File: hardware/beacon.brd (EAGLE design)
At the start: 65.5 x 96.5 mm, 26 parts, among them IC1 LM1117SX-3.3, Q1 BC850SMD, Q2 BC850SMD, Q3 12MHz, U1 ESP-12F, X1 MINI-USB-UX60A-MB-5ST

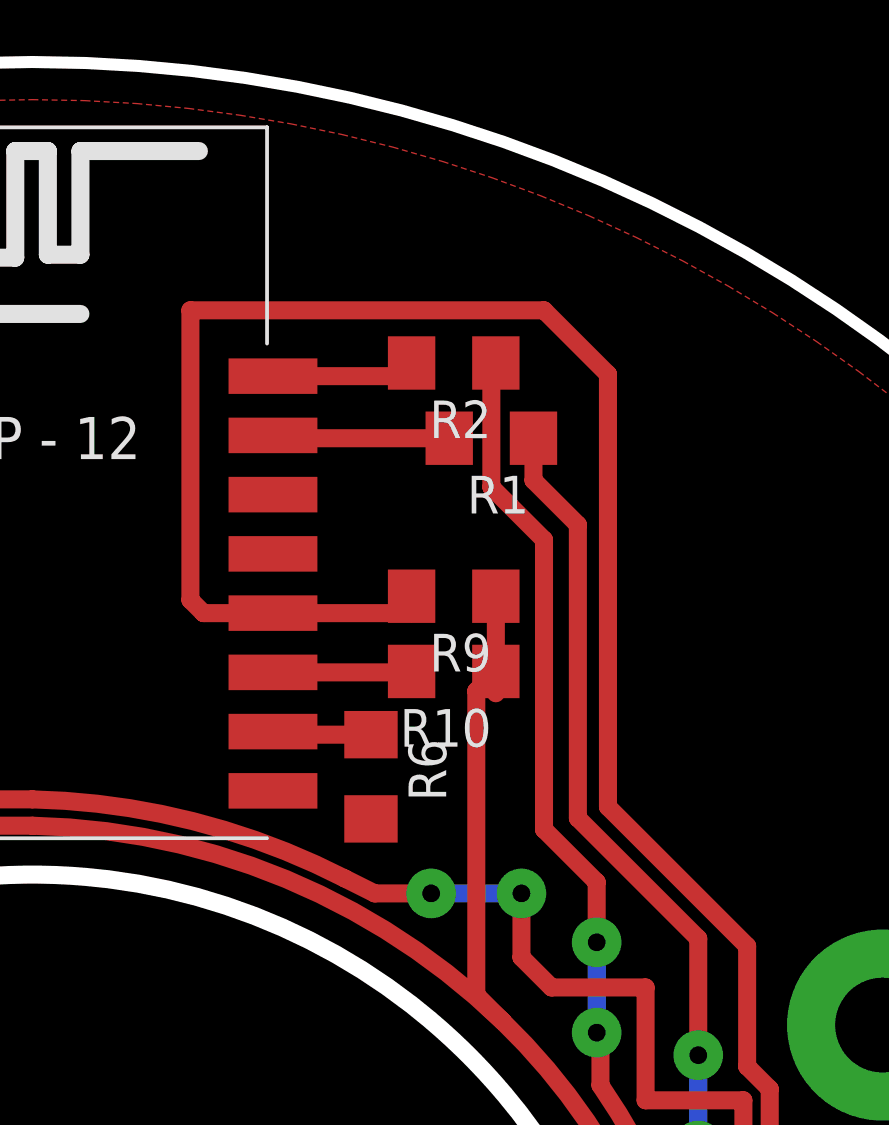
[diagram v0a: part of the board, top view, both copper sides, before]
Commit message: add test pads
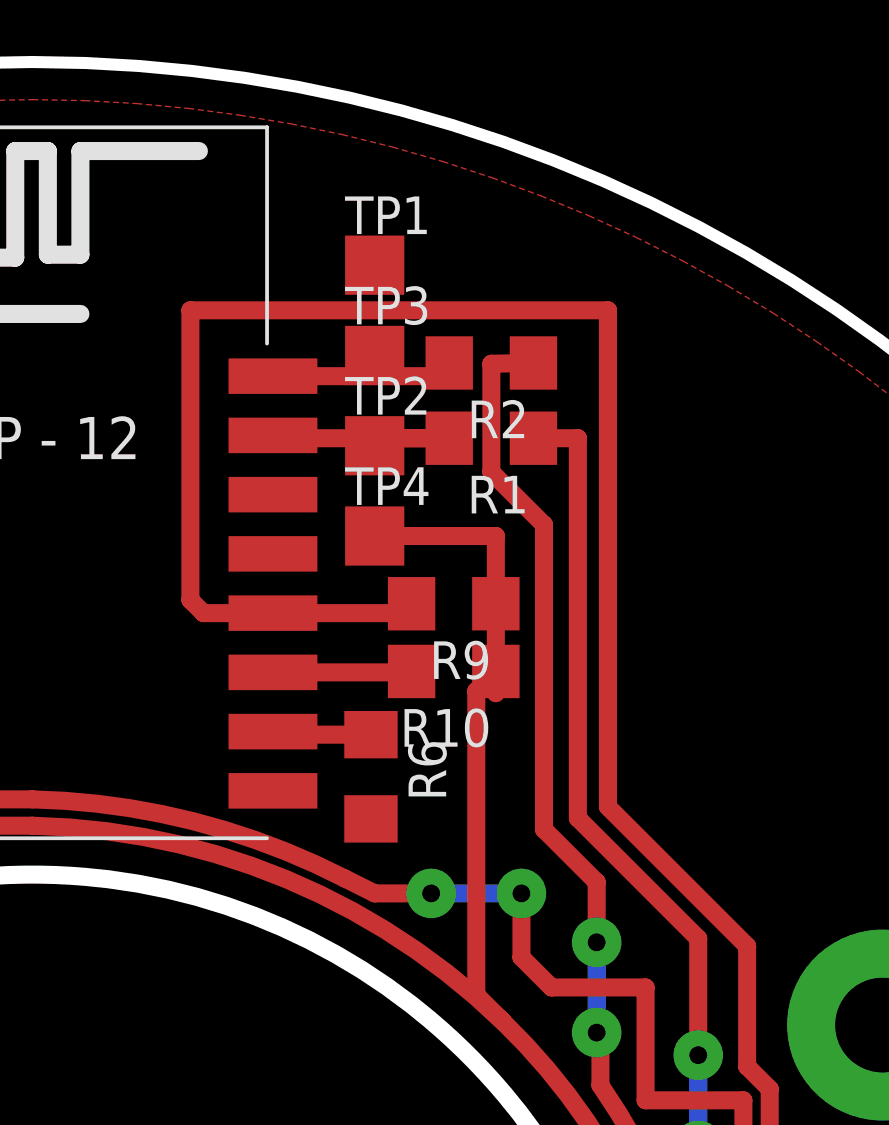
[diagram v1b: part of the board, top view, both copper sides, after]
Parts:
- added TP1, TP2, TP3, TP4: TPSQTP20SQ, testpad:TP20SQ
- moved R2 1.27 mm to (15.5, 38.1)
- moved R9 0.25 mm to (14.2, 30.0)
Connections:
- net +3V3: now also TP4.TP
- net GND: now also TP1.TP
- net RX: now also TP3.TP
- net TX: now also TP2.TP
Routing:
- net +3V3: track 221.6 -> 227.7 mm
- net TX: track 6.05 -> 8.81 mm
- net RX: track 5.12 -> 7.08 mm
- net N$2: track 85.8 -> 87.1 mm
- net GPIO0: track 109.4 -> 110.4 mm
- net N$1: track 82.8 -> 83.7 mm
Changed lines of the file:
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@@
 <element name="R1" library="rcl" package="R1206" value="470" x="15.494" y="35.56" rot="R180"/>
 <element name="R10" library="rcl" package="R1206" value="10k" x="14.224" y="27.686" rot="R180"/>
-<element name="R2" library="rcl" package="R1206" value="470" x="14.224" y="38.1" rot="R180"/>
+<element name="R2" library="rcl" package="R1206" value="470" x="15.494" y="38.1" rot="R180"/>
 <element name="R4" library="rcl" package="R1206" value="10k" x="26.1366" y="-34.9758" rot="R90"/>
 <element name="R5" library="rcl" package="R1206" value="10k" x="22.987" y="-37.211" rot="R90"/>
@@
 <element name="R7" library="rcl" package="R1206" value="10k" x="-13.589" y="30.988"/>
 <element name="R8" library="rcl" package="R1206" value="10k" x="-13.589" y="35.56"/>
-<element name="R9" library="rcl" package="R1206" value="10k" x="14.224" y="30.226" rot="R180"/>
+<element name="R9" library="rcl" package="R1206" value="10k" x="14.224" y="29.972" rot="R180"/>
 <element name="RESET" library="switch-omron" package="B3F-10XX" value="" x="-14.989309375" y="41.125021875" rot="R200">
 <attribute name="MF" value="" x="-14.989309375" y="41.125021875" size="1.778" layer="27" rot="R200" display="off"/>
@@
 <attribute name="OC_FARNELL" value="unknown" x="0" y="-41.91" size="1.778" layer="27" rot="R90" display="off"/>
 <attribute name="OC_NEWARK" value="unknown" x="0" y="-41.91" size="1.778" layer="27" rot="R90" display="off"/>
+</element>
+<element name="TP1" library="testpad" package="TP20SQ" value="TPSQTP20SQ" x="11.557" y="41.402">
+<attribute name="TP_SIGNAL_NAME" value="" x="11.557" y="41.402" size="1.778" layer="27" display="off"/>
+</element>
+<element name="TP2" library="testpad" package="TP20SQ" value="TPSQTP20SQ" x="11.557" y="35.306">
+<attribute name="TP_SIGNAL_NAME" value="" x="11.557" y="35.306" size="1.778" layer="27" display="off"/>
+</element>
+<element name="TP3" library="testpad" package="TP20SQ" value="TPSQTP20SQ" x="11.557" y="38.354">
+<attribute name="TP_SIGNAL_NAME" value="" x="11.557" y="38.354" size="1.778" layer="27" display="off"/>
+</element>
+<element name="TP4" library="testpad" package="TP20SQ" value="TPSQTP20SQ" x="11.557" y="32.258">
+<attribute name="TP_SIGNAL_NAME" value="" x="11.557" y="32.258" size="1.778" layer="27" display="off"/>
 </element>
 </elements>
@@
 <wire x1="9.906" y1="-40.64" x2="6.858" y2="-40.64" width="0.6096" layer="16"/>
 <via x="6.858" y="-40.64" extent="1-16" drill="0.6" diameter="1.6764" shape="square"/>
+<contactref element="TP1" pad="TP"/>
 </signal>
 <signal name="+3V3">
@@
 <wire x1="-15.011" y1="30.988" x2="-15.011" y2="35.56" width="0.6096" layer="1"/>
 <wire x1="15.646" y1="26.949" x2="15.646" y2="27.686" width="0.6096" layer="1"/>
-<wire x1="15.646" y1="27.686" x2="15.646" y2="30.226" width="0.6096" layer="1"/>
+<wire x1="15.646" y1="27.686" x2="15.646" y2="29.972" width="0.6096" layer="1"/>
 <wire x1="15.646" y1="27.686" x2="14.986" y2="27.026" width="0.6096" layer="1"/>
 <wire x1="14.986" y1="16.764" x2="15.875" y2="15.875" width="0.6096" layer="1"/>
 <wire x1="14.986" y1="27.026" x2="14.986" y2="16.764" width="0.6096" layer="1"/>
+<contactref element="TP4" pad="TP"/>
+<wire x1="15.646" y1="29.972" x2="15.646" y2="32.258" width="0.6096" layer="1"/>
+<wire x1="15.646" y1="32.258" x2="11.557" y2="32.258" width="0.6096" layer="1"/>
 </signal>
 <signal name="+5V">
@@
 <contactref element="U1" pad="TXD0"/>
 <contactref element="R2" pad="2"/>
-<wire x1="12.802" y1="38.1" x2="12.802" y2="37.655215625" width="0.6096" layer="1"/>
-<wire x1="12.802" y1="37.655215625" x2="8.121790625" y2="37.655215625" width="0.6096" layer="1"/>
+<wire x1="13.437" y1="37.655215625" x2="14.072" y2="38.1" width="0.6096" layer="1"/>
+<wire x1="12.255784375" y1="37.655215625" x2="8.121790625" y2="37.655215625" width="0.6096" layer="1"/>
+<contactref element="TP3" pad="TP"/>
+<wire x1="11.557" y1="38.354" x2="12.255784375" y2="37.655215625" width="0.6096" layer="1"/>
+<wire x1="12.255784375" y1="37.655215625" x2="13.437" y2="37.655215625" width="0.6096" layer="1"/>
 </signal>
 <signal name="TX">
@@
 <contactref element="R1" pad="2"/>
 <wire x1="8.121790625" y1="35.655215625" x2="8.121790625" y2="35.56" width="0.6096" layer="1"/>
-<wire x1="8.121790625" y1="35.56" x2="14.072" y2="35.56" width="0.6096" layer="1"/>
+<wire x1="14.072" y1="35.56" x2="8.121790625" y2="35.56" width="0.6096" layer="1"/>
+<contactref element="TP2" pad="TP"/>
+<wire x1="11.557" y1="35.306" x2="11.557" y2="35.56" width="0.6096" layer="1"/>
+<wire x1="11.557" y1="35.56" x2="14.072" y2="35.56" width="0.6096" layer="1"/>
 </signal>
 <signal name="TRIGGER">
@@
 <wire x1="20.7518" y1="-15.2146" x2="26.162" y2="0" width="0.6096" layer="1" curve="38.831966"/>
 <wire x1="8.121790625" y1="29.655215625" x2="12.802" y2="29.655215625" width="0.6096" layer="1"/>
-<wire x1="12.802" y1="30.226" x2="12.802" y2="29.655215625" width="0.6096" layer="1"/>
+<wire x1="12.802" y1="29.972" x2="12.802" y2="29.655215625" width="0.6096" layer="1"/>
 <wire x1="26.162" y1="0" x2="24.892" y2="8.255" width="0.6096" layer="1" curve="17.810377"/>
-<wire x1="19.431" y1="23.114" x2="19.431" y2="37.719" width="0.6096" layer="1"/>
-<wire x1="19.431" y1="37.719" x2="17.272" y2="39.878" width="0.6096" layer="1"/>
-<wire x1="17.272" y1="39.878" x2="5.334" y2="39.878" width="0.6096" layer="1"/>
+<wire x1="19.431" y1="23.114" x2="19.431" y2="39.878" width="0.6096" layer="1"/>
+<wire x1="19.431" y1="39.878" x2="5.334" y2="39.878" width="0.6096" layer="1"/>
 <wire x1="5.334" y1="39.878" x2="5.334" y2="30.099" width="0.6096" layer="1"/>
 <wire x1="5.334" y1="30.099" x2="5.777784375" y2="29.655215625" width="0.6096" layer="1"/>
@@
 <wire x1="22.479" y1="11.684" x2="22.479" y2="14.732" width="0.6096" layer="16"/>
 <via x="22.479" y="14.732" extent="1-16" drill="0.6" diameter="1.6764" shape="square"/>
-<wire x1="18.415" y1="32.639" x2="18.415" y2="22.733" width="0.6096" layer="1"/>
-<wire x1="16.916" y1="34.138" x2="16.916" y2="35.56" width="0.6096" layer="1"/>
-<wire x1="18.415" y1="32.639" x2="16.916" y2="34.138" width="0.6096" layer="1"/>
-<wire x1="18.415" y1="22.733" x2="22.479" y2="18.669" width="0.6096" layer="1"/>
+<wire x1="22.479" y1="18.669" x2="18.415" y2="22.733" width="0.6096" layer="1"/>
 <wire x1="22.479" y1="18.669" x2="22.479" y2="14.732" width="0.6096" layer="1"/>
+<wire x1="18.415" y1="35.56" x2="16.916" y2="35.56" width="0.6096" layer="1"/>
+<wire x1="18.415" y1="22.733" x2="18.415" y2="35.56" width="0.6096" layer="1"/>
 </signal>
 <signal name="N$2">
@@
 <via x="19.05" y="18.542" extent="1-16" drill="0.6" diameter="1.6764" shape="square"/>
 <wire x1="19.05" y1="18.542" x2="19.05" y2="20.574" width="0.6096" layer="1"/>
-<wire x1="15.494" y1="37.948" x2="15.646" y2="38.1" width="0.6096" layer="1"/>
-<wire x1="19.05" y1="20.574" x2="17.272" y2="22.352" width="0.6096" layer="1"/>
-<wire x1="17.272" y1="22.352" x2="17.272" y2="32.131" width="0.6096" layer="1"/>
-<wire x1="17.272" y1="32.131" x2="15.494" y2="33.909" width="0.6096" layer="1"/>
-<wire x1="15.494" y1="33.909" x2="15.494" y2="37.948" width="0.6096" layer="1"/>
+<wire x1="15.494" y1="38.075" x2="16.916" y2="38.1" width="0.6096" layer="1"/>
+<wire x1="17.272" y1="22.352" x2="19.05" y2="20.574" width="0.6096" layer="1"/>
+<wire x1="15.494" y1="38.075" x2="15.494" y2="34.417" width="0.6096" layer="1"/>
+<wire x1="15.494" y1="34.417" x2="17.272" y2="32.639" width="0.6096" layer="1"/>
+<wire x1="17.272" y1="32.639" x2="17.272" y2="22.352" width="0.6096" layer="1"/>
 </signal>
 <signal name="N$3">
